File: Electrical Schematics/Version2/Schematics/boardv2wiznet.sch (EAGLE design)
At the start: 9 parts

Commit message: Connected Ethernet Connector
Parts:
- added C3, C4, C5: 0.1, eagle-ltspice:CC0603
- added R2, R3, R8, R9: 51, SparkFun-Passives:RESISTOR0603-RES
- added R4, R5: 200, SparkFun-Passives:RESISTOR0603-RES
- added U$1: ETHERNET_CONNECTOR, shit:ETHERNET_CONNECTOR
- C29, C30, C31, C32, C33, C34, C41: device rcl:C-EUC0603 -> eagle-ltspice:CC0603
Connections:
- net N$47 renamed P$2_CLK_TO_XTLP_WIZNET
- net N$48 renamed P$1_CLK_TO_XTLN_WIZNET
- new net 0.1: R3.2, U2.TXOP
- new net N$1: C3.1, R2.2, R3.1
- new net N$10: U$1.L4, U2.FDXLED
- new net N$12: R8.2, U$1.R8, U2.RXIP
- new net N$2: U$1.L2, U2.LINKLED
- new net N$4: C5.1, R8.1, R9.2
- new net N$5: R2.1, U$1.R2, U2.TXON
- new net N$6: R4.1, U$1.L1
- new net N$7: R5.1, U$1.L3
- new net N$9: R9.1, U$1.R7, U2.RXIN
- new net WIZNET_TO_GND: U2.GNDA@0, U2.GNDA@2, U2.GNDD@0, U2.GNDD@1, U2.GNDD@2, U2.GNDD@3, U2.GNDD@4, U2.GNDD@5, U2.TEST0, U2.TEST1, U2.TEST2, U2.TEST3
- net GND: now also C3.2, C4.2, C5.2; no longer U2.GNDA@0, U2.GNDA@2, U2.GNDD@0, U2.GNDD@1, U2.GNDD@2, U2.GNDD@3, U2.GNDD@4, U2.GNDD@5, U2.TEST0, U2.TEST1, U2.TEST2, U2.TEST3
- net N$45: now also C4.1, R4.2, R5.2
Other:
- moved on the sheet: C30, C31, C41

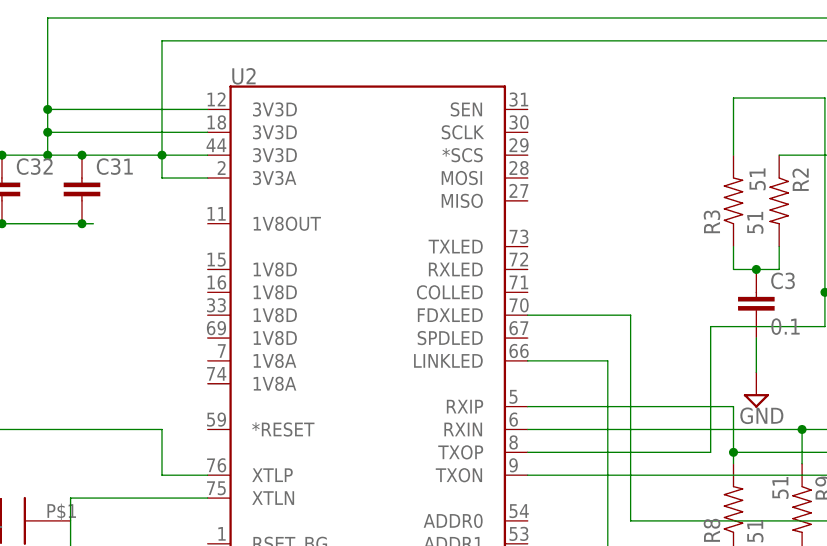
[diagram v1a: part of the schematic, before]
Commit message: updated power ethernet and tempatature
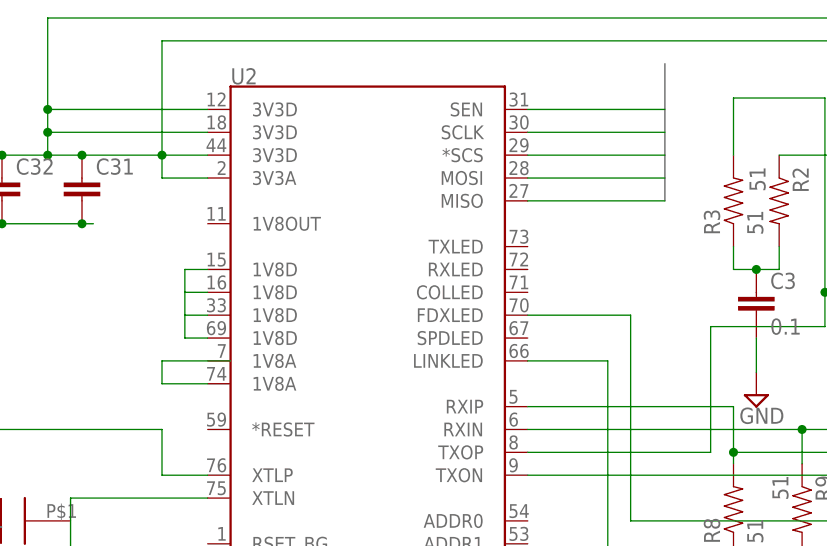
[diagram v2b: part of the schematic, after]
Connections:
- new net B$1: U2.*SCS, U2.MISO, U2.MOSI, U2.SCLK, U2.SEN
- new net N$3: U2.1V8A@1
- new net N$8: U2.1V8D@0, U2.1V8D@1, U2.1V8D@2, U2.1V8D@3
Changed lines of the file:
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@@
 <setting verticaltext="up"/>
 </settings>
-<grid distance="0.05" unitdist="inch" unit="inch" style="lines" multiple="1" display="no" altdistance="0.025" altunitdist="inch" altunit="inch"/>
+<grid distance="0.1" unitdist="inch" unit="inch" style="lines" multiple="1" display="no" altdistance="0.01" altunitdist="inch" altunit="inch"/>
 <layers>
-<layer number="1" name="Top" color="4" fill="1" visible="yes" active="no"/>
-<layer number="2" name="Route2" color="1" fill="3" visible="yes" active="no"/>
-<layer number="3" name="Route3" color="4" fill="3" visible="yes" active="no"/>
-<layer number="4" name="Route4" color="1" fill="4" visible="yes" active="no"/>
-<layer number="5" name="Route5" color="4" fill="4" visible="yes" active="no"/>
-<layer number="6" name="Route6" color="1" fill="8" visible="yes" active="no"/>
-<layer number="7" name="Route7" color="4" fill="8" visible="yes" active="no"/>
-<layer number="8" name="Route8" color="1" fill="2" visible="yes" active="no"/>
-<layer number="9" name="Route9" color="4" fill="2" visible="yes" active="no"/>
-<layer number="10" name="Route10" color="1" fill="7" visible="yes" active="no"/>
-<layer number="11" name="Route11" color="4" fill="7" visible="yes" active="no"/>
-<layer number="12" name="Route12" color="1" fill="5" visible="yes" active="no"/>
-<layer number="13" name="Route13" color="4" fill="5" visible="yes" active="no"/>
-<layer number="14" name="Route14" color="1" fill="6" visible="yes" active="no"/>
-<layer number="15" name="Route15" color="4" fill="6" visible="yes" active="no"/>
-<layer number="16" name="Bottom" color="1" fill="1" visible="yes" active="no"/>
-<layer number="17" name="Pads" color="2" fill="1" visible="yes" active="no"/>
-<layer number="18" name="Vias" color="2" fill="1" visible="yes" active="no"/>
-<layer number="19" name="Unrouted" color="6" fill="1" visible="yes" active="no"/>
-<layer number="20" name="Dimension" color="15" fill="1" visible="yes" active="no"/>
-<layer number="21" name="tPlace" color="7" fill="1" visible="yes" active="no"/>
-<layer number="22" name="bPlace" color="7" fill="1" visible="yes" active="no"/>
-<layer number="23" name="tOrigins" color="15" fill="1" visible="yes" active="no"/>
-<layer number="24" name="bOrigins" color="15" fill="1" visible="yes" active="no"/>
-<layer number="25" name="tNames" color="7" fill="1" visible="yes" active="no"/>
-<layer number="26" name="bNames" color="7" fill="1" visible="yes" active="no"/>
-<layer number="27" name="tValues" color="7" fill="1" visible="yes" active="no"/>
-<layer number="28" name="bValues" color="7" fill="1" visible="yes" active="no"/>
+<layer number="1" name="Top" color="4" fill="1" visible="no" active="no"/>
+<layer number="2" name="Route2" color="1" fill="3" visible="no" active="no"/>
+<layer number="3" name="Route3" color="4" fill="3" visible="no" active="no"/>
+<layer number="4" name="Route4" color="1" fill="4" visible="no" active="no"/>
+<layer number="5" name="Route5" color="4" fill="4" visible="no" active="no"/>
+<layer number="6" name="Route6" color="1" fill="8" visible="no" active="no"/>
+<layer number="7" name="Route7" color="4" fill="8" visible="no" active="no"/>
+<layer number="8" name="Route8" color="1" fill="2" visible="no" active="no"/>
+<layer number="9" name="Route9" color="4" fill="2" visible="no" active="no"/>
+<layer number="10" name="Route10" color="1" fill="7" visible="no" active="no"/>
+<layer number="11" name="Route11" color="4" fill="7" visible="no" active="no"/>
+<layer number="12" name="Route12" color="1" fill="5" visible="no" active="no"/>
+<layer number="13" name="Route13" color="4" fill="5" visible="no" active="no"/>
+<layer number="14" name="Route14" color="1" fill="6" visible="no" active="no"/>
+<layer number="15" name="Route15" color="4" fill="6" visible="no" active="no"/>
+<layer number="16" name="Bottom" color="1" fill="1" visible="no" active="no"/>
+<layer number="17" name="Pads" color="2" fill="1" visible="no" active="no"/>
+<layer number="18" name="Vias" color="2" fill="1" visible="no" active="no"/>
+<layer number="19" name="Unrouted" color="6" fill="1" visible="no" active="no"/>
+<layer number="20" name="Dimension" color="15" fill="1" visible="no" active="no"/>
+<layer number="21" name="tPlace" color="7" fill="1" visible="no" active="no"/>
+<layer number="22" name="bPlace" color="7" fill="1" visible="no" active="no"/>
+<layer number="23" name="tOrigins" color="15" fill="1" visible="no" active="no"/>
+<layer number="24" name="bOrigins" color="15" fill="1" visible="no" active="no"/>
+<layer number="25" name="tNames" color="7" fill="1" visible="no" active="no"/>
+<layer number="26" name="bNames" color="7" fill="1" visible="no" active="no"/>
+<layer number="27" name="tValues" color="7" fill="1" visible="no" active="no"/>
+<layer number="28" name="bValues" color="7" fill="1" visible="no" active="no"/>
 <layer number="29" name="tStop" color="7" fill="3" visible="no" active="no"/>
 <layer number="30" name="bStop" color="7" fill="6" visible="no" active="no"/>
@@
 <layer number="35" name="tGlue" color="7" fill="4" visible="no" active="no"/>
 <layer number="36" name="bGlue" color="7" fill="5" visible="no" active="no"/>
-<layer number="37" name="tTest" color="7" fill="1" visible="yes" active="no"/>
-<layer number="38" name="bTest" color="7" fill="1" visible="yes" active="no"/>
+<layer number="37" name="tTest" color="7" fill="1" visible="no" active="no"/>
+<layer number="38" name="bTest" color="7" fill="1" visible="no" active="no"/>
 <layer number="39" name="tKeepout" color="4" fill="11" visible="no" active="no"/>
 <layer number="40" name="bKeepout" color="1" fill="11" visible="no" active="no"/>
@@
 <layer number="44" name="Drills" color="7" fill="1" visible="no" active="no"/>
 <layer number="45" name="Holes" color="7" fill="1" visible="no" active="no"/>
-<layer number="46" name="Milling" color="3" fill="1" visible="yes" active="no"/>
-<layer number="47" name="Measures" color="7" fill="1" visible="yes" active="no"/>
-<layer number="48" name="Document" color="7" fill="1" visible="yes" active="no"/>
-<layer number="49" name="Reference" color="7" fill="1" visible="yes" active="no"/>
-<layer number="50" name="dxf" color="7" fill="1" visible="yes" active="no"/>
-<layer number="51" name="tDocu" color="7" fill="1" visible="yes" active="no"/>
-<layer number="52" name="bDocu" color="7" fill="1" visible="yes" active="no"/>
-<layer number="53" name="tGND_GNDA" color="7" fill="9" visible="yes" active="no"/>
-<layer number="54" name="bGND_GNDA" color="1" fill="9" visible="yes" active="no"/>
-<layer number="56" name="wert" color="7" fill="1" visible="yes" active="no"/>
-<layer number="57" name="tCAD" color="7" fill="1" visible="yes" active="no"/>
+<layer number="46" name="Milling" color="3" fill="1" visible="no" active="no"/>
+<layer number="47" name="Measures" color="7" fill="1" visible="no" active="no"/>
+<layer number="48" name="Document" color="7" fill="1" visible="no" active="no"/>
+<layer number="49" name="Reference" color="7" fill="1" visible="no" active="no"/>
+<layer number="50" name="dxf" color="7" fill="1" visible="no" active="no"/>
+<layer number="51" name="tDocu" color="7" fill="1" visible="no" active="no"/>
+<layer number="52" name="bDocu" color="7" fill="1" visible="no" active="no"/>
+<layer number="53" name="tGND_GNDA" color="7" fill="9" visible="no" active="no"/>
+<layer number="54" name="bGND_GNDA" color="1" fill="9" visible="no" active="no"/>
+<layer number="56" name="wert" color="7" fill="1" visible="no" active="no"/>
+<layer number="57" name="tCAD" color="7" fill="1" visible="no" active="no"/>
 <layer number="90" name="Modules" color="5" fill="1" visible="yes" active="yes"/>
 <layer number="91" name="Nets" color="2" fill="1" visible="yes" active="yes"/>
@@
 </instances>
 <busses>
+<bus name="B$1">
+<segment>
+<wire x1="86.36" y1="101.6" x2="86.36" y2="116.84" width="0.762" layer="92"/>
+</segment>
+</bus>
 </busses>
 <nets>
@@
 </segment>
 </net>
+<net name="B$1" class="0">
+<segment>
+<pinref part="U2" gate="G$1" pin="SEN"/>
+<wire x1="86.36" y1="111.76" x2="71.12" y2="111.76" width="0.1524" layer="91"/>
+</segment>
+<segment>
+<pinref part="U2" gate="G$1" pin="SCLK"/>
+<wire x1="86.36" y1="109.22" x2="71.12" y2="109.22" width="0.1524" layer="91"/>
+</segment>
+<segment>
+<pinref part="U2" gate="G$1" pin="*SCS"/>
+<wire x1="86.36" y1="106.68" x2="71.12" y2="106.68" width="0.1524" layer="91"/>
+</segment>
+<segment>
+<pinref part="U2" gate="G$1" pin="MOSI"/>
+<wire x1="86.36" y1="104.14" x2="71.12" y2="104.14" width="0.1524" layer="91"/>
+</segment>
+<segment>
+<pinref part="U2" gate="G$1" pin="MISO"/>
+<wire x1="86.36" y1="101.6" x2="71.12" y2="101.6" width="0.1524" layer="91"/>
+</segment>
+</net>
+<net name="N$3" class="0">
+<segment>
+<pinref part="U2" gate="G$1" pin="1V8A@1"/>
+<wire x1="35.56" y1="81.28" x2="30.48" y2="81.28" width="0.1524" layer="91"/>
+<wire x1="30.48" y1="81.28" x2="30.48" y2="83.82" width="0.1524" layer="91"/>
+<wire x1="30.48" y1="83.82" x2="38.1" y2="83.82" width="0.1524" layer="91"/>
+</segment>
+</net>
+<net name="N$8" class="0">
+<segment>
+<pinref part="U2" gate="G$1" pin="1V8D@3"/>
+<wire x1="35.56" y1="86.36" x2="33.02" y2="86.36" width="0.1524" layer="91"/>
+<wire x1="33.02" y1="86.36" x2="33.02" y2="88.9" width="0.1524" layer="91"/>
+<pinref part="U2" gate="G$1" pin="1V8D@2"/>
+<wire x1="33.02" y1="88.9" x2="35.56" y2="88.9" width="0.1524" layer="91"/>
+<pinref part="U2" gate="G$1" pin="1V8D@1"/>
+<wire x1="35.56" y1="91.44" x2="33.02" y2="91.44" width="0.1524" layer="91"/>
+<wire x1="33.02" y1="91.44" x2="33.02" y2="88.9" width="0.1524" layer="91"/>
+<pinref part="U2" gate="G$1" pin="1V8D@0"/>
+<wire x1="35.56" y1="93.98" x2="33.02" y2="93.98" width="0.1524" layer="91"/>
+<wire x1="33.02" y1="93.98" x2="33.02" y2="91.44" width="0.1524" layer="91"/>
+</segment>
+</net>

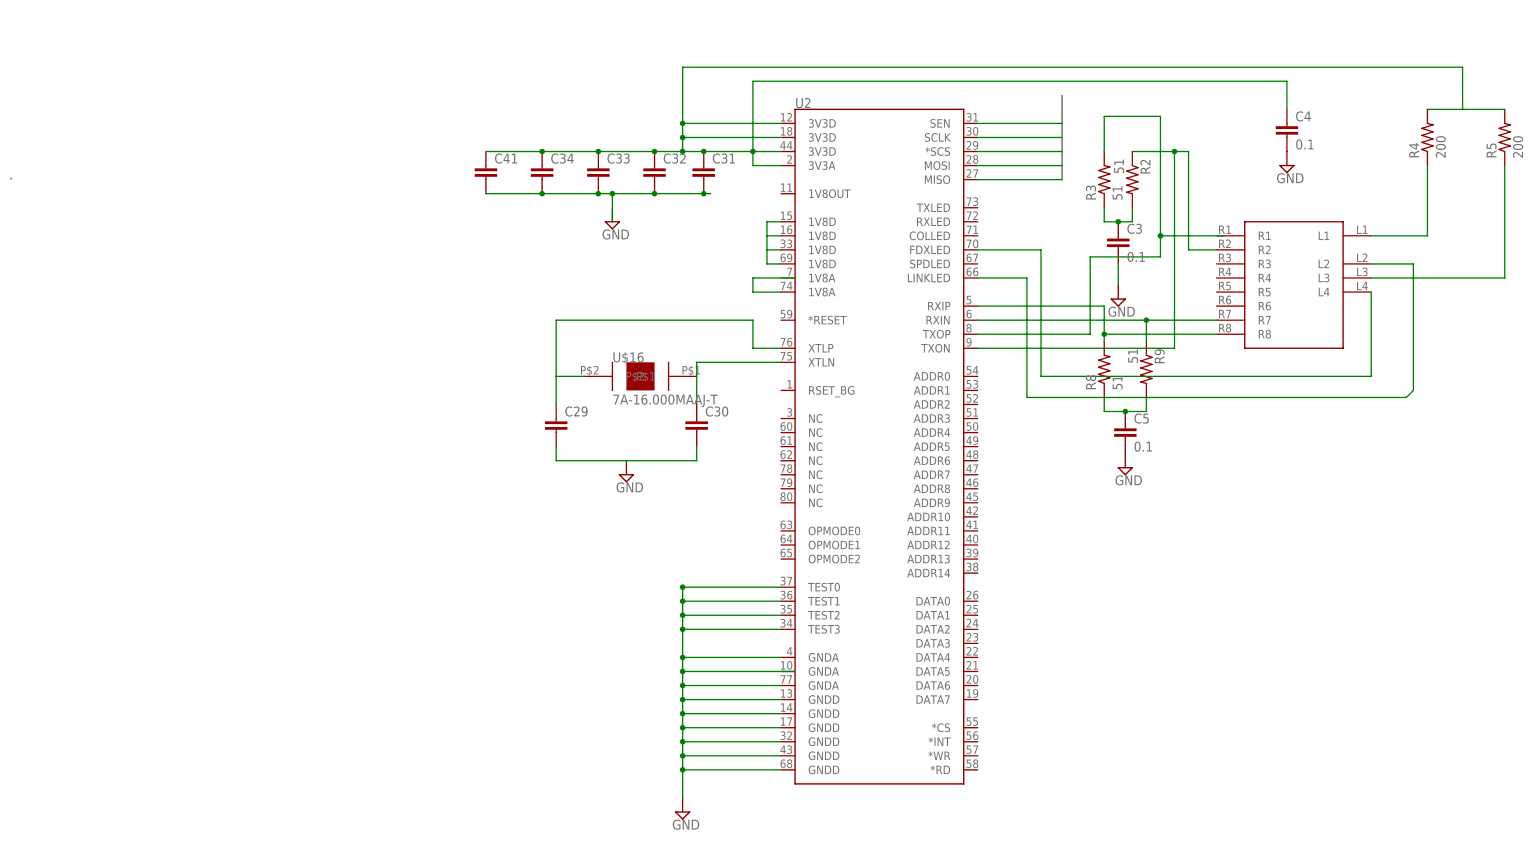
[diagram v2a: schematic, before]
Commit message: updated the schematics for the ridgley
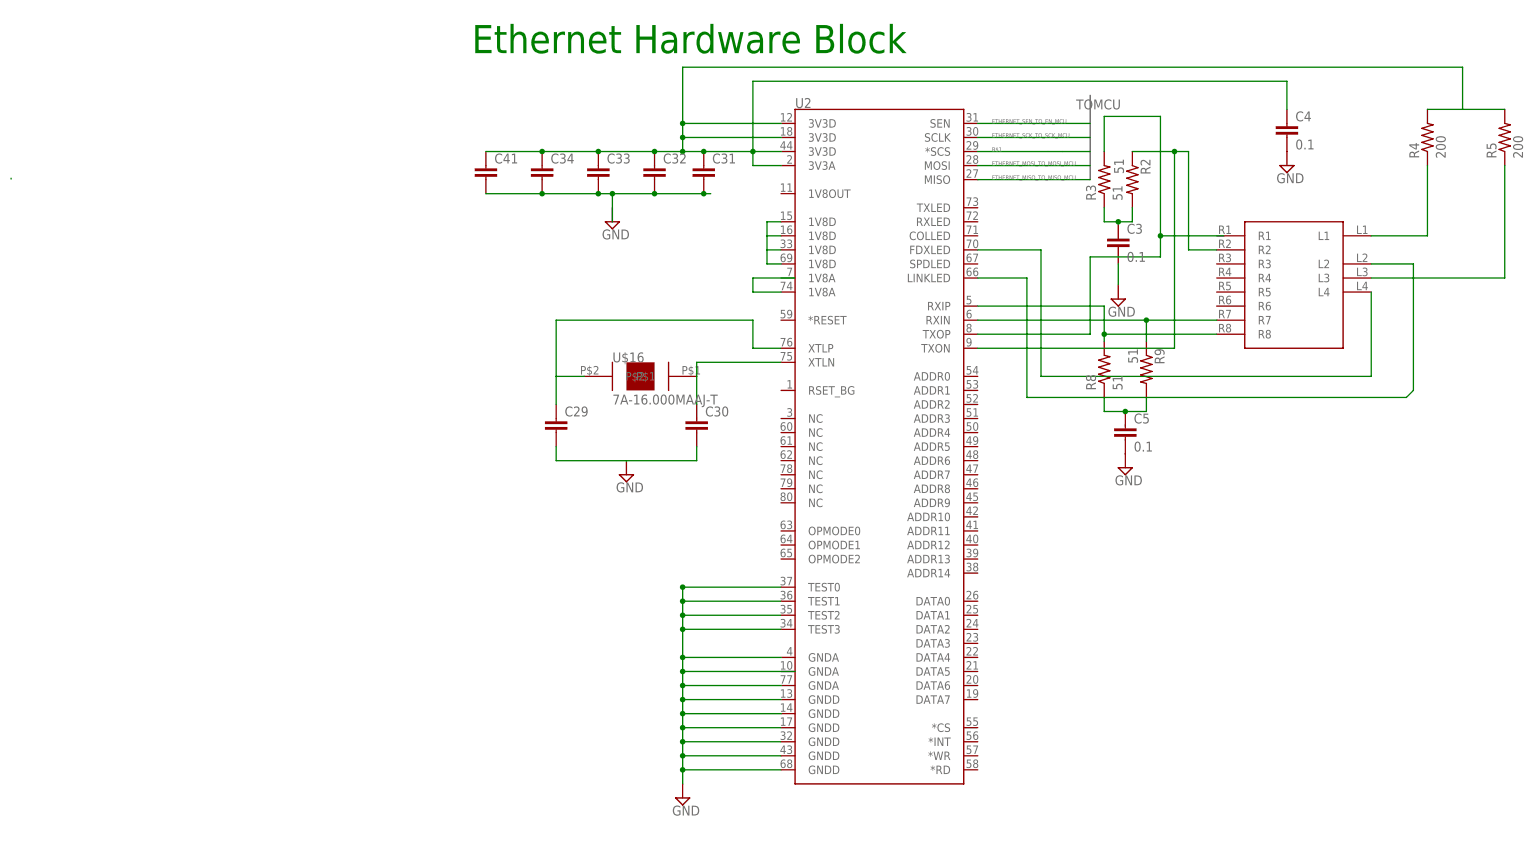
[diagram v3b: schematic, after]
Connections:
- new net ETHERNET_MISO_TO_MISO_MCU: U2.MISO
- new net ETHERNET_MOSI_TO_MOSI_MCU: U2.MOSI
- new net ETHERNET_SCK_TO_SCK_MCU: U2.SCLK
- new net ETHERNET_SEN_TO_EN_MCU: U2.SEN
- net B$1: no longer U2.MISO, U2.MOSI, U2.SCLK, U2.SEN
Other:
- note added: "Ethernet Hardware Block"
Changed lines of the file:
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@@
 <part name="C32" library="eagle-ltspice" deviceset="C" device="C0603"/>
 <part name="C41" library="eagle-ltspice" deviceset="C" device="C0603"/>
+<part name="FRAME1" library="frames" deviceset="DOCFIELD" device=""/>
 </parts>
 <sheets>
 <sheet>
 <plain>
+<frame x1="-33.02" y1="-17.78" x2="198.12" y2="134.62" columns="8" rows="5" layer="91"/>
+<text x="-20.32" y="124.46" size="5.08" layer="91">Ethernet Hardware Block</text>
 </plain>
 <instances>
@@
 <instance part="U$16" gate="G$1" x="10.16" y="66.04"/>
 <instance part="SUPPLY7" gate="GND" x="7.62" y="48.26"/>
-<instance part="SUPPLY8" gate="GND" x="17.78" y="-12.7"/>
+<instance part="SUPPLY8" gate="GND" x="17.78" y="-10.16"/>
 <instance part="SUPPLY9" gate="GND" x="5.08" y="93.98"/>
 <instance part="R2" gate="G$1" x="99.06" y="101.6" rot="R270"/>
@@
 <instance part="C32" gate="G$1" x="12.7" y="104.14"/>
 <instance part="C41" gate="G$1" x="-17.78" y="104.14"/>
+<instance part="FRAME1" gate="G$1" x="88.9" y="-12.7"/>
 </instances>
 <busses>
-<bus name="B$1">
-<segment>
-<wire x1="86.36" y1="101.6" x2="86.36" y2="116.84" width="0.762" layer="92"/>
+<bus name="TOMCU">
+<segment>
+<wire x1="91.44" y1="101.6" x2="91.44" y2="116.84" width="0.762" layer="92"/>
+<label x="88.9" y="114.3" size="1.778" layer="95"/>
 </segment>
 </bus>
@@
 <wire x1="17.78" y1="0" x2="17.78" y2="-2.54" width="0.1524" layer="91"/>
 <wire x1="17.78" y1="-2.54" x2="17.78" y2="-5.08" width="0.1524" layer="91"/>
-<wire x1="17.78" y1="-5.08" x2="17.78" y2="-10.16" width="0.1524" layer="91"/>
+<wire x1="17.78" y1="-5.08" x2="17.78" y2="-7.62" width="0.1524" layer="91"/>
 <wire x1="38.1" y1="12.7" x2="17.78" y2="12.7" width="0.1524" layer="91"/>
 <wire x1="17.78" y1="12.7" x2="17.78" y2="10.16" width="0.1524" layer="91"/>
@@
 <net name="B$1" class="0">
 <segment>
-<pinref part="U2" gate="G$1" pin="SEN"/>
-<wire x1="86.36" y1="111.76" x2="71.12" y2="111.76" width="0.1524" layer="91"/>
-</segment>
-<segment>
-<pinref part="U2" gate="G$1" pin="SCLK"/>
-<wire x1="86.36" y1="109.22" x2="71.12" y2="109.22" width="0.1524" layer="91"/>
-</segment>
-<segment>
 <pinref part="U2" gate="G$1" pin="*SCS"/>
-<wire x1="86.36" y1="106.68" x2="71.12" y2="106.68" width="0.1524" layer="91"/>
-</segment>
-<segment>
-<pinref part="U2" gate="G$1" pin="MOSI"/>
-<wire x1="86.36" y1="104.14" x2="71.12" y2="104.14" width="0.1524" layer="91"/>
-</segment>
-<segment>
-<pinref part="U2" gate="G$1" pin="MISO"/>
-<wire x1="86.36" y1="101.6" x2="71.12" y2="101.6" width="0.1524" layer="91"/>
+<wire x1="86.36" y1="106.68" x2="83.82" y2="106.68" width="0.1524" layer="91"/>
+<label x="73.66" y="106.68" size="0.762" layer="95"/>
+<wire x1="83.82" y1="106.68" x2="71.12" y2="106.68" width="0.1524" layer="91"/>
+<wire x1="86.36" y1="106.68" x2="91.44" y2="106.68" width="0.1524" layer="91"/>
 </segment>
 </net>
@@
 </segment>
 </net>
+<net name="ETHERNET_SEN_TO_EN_MCU" class="0">
+<segment>
+<pinref part="U2" gate="G$1" pin="SEN"/>
+<wire x1="91.44" y1="111.76" x2="71.12" y2="111.76" width="0.1524" layer="91"/>
+<label x="73.66" y="111.76" size="0.762" layer="95"/>
+</segment>
+</net>
+<net name="ETHERNET_SCK_TO_SCK_MCU" class="0">
+<segment>
+<pinref part="U2" gate="G$1" pin="SCLK"/>
+<wire x1="91.44" y1="109.22" x2="71.12" y2="109.22" width="0.1524" layer="91"/>
+<label x="73.66" y="109.22" size="0.762" layer="95"/>
+</segment>
+</net>
+<net name="ETHERNET_MOSI_TO_MOSI_MCU" class="0">
+<segment>
+<pinref part="U2" gate="G$1" pin="MOSI"/>
+<wire x1="91.44" y1="104.14" x2="71.12" y2="104.14" width="0.1524" layer="91"/>
+<label x="73.66" y="104.14" size="0.762" layer="95"/>
+</segment>
+</net>
+<net name="ETHERNET_MISO_TO_MISO_MCU" class="0">
+<segment>
+<pinref part="U2" gate="G$1" pin="MISO"/>
+<wire x1="91.44" y1="101.6" x2="71.12" y2="101.6" width="0.1524" layer="91"/>
+<label x="73.66" y="101.6" size="0.762" layer="95"/>
+</segment>
+</net>
